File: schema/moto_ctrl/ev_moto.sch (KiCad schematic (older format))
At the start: 131 parts, among them J4 DB37, P7 CONN_6X2, P8 CONN_2, P9 SWD-IAP, Q1 MOSFET_P, Q2 MOSFET_N, Q3 NPN, Q4 MOSFET_P, Q5 NPN, Q6 MOSFET_N, U3 NCP3063, X2 8MHz

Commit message: Made switchable USB.
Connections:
- net labels added: usb-en
- wire segments 457 -> 458
- no-connect marks 17 -> 16

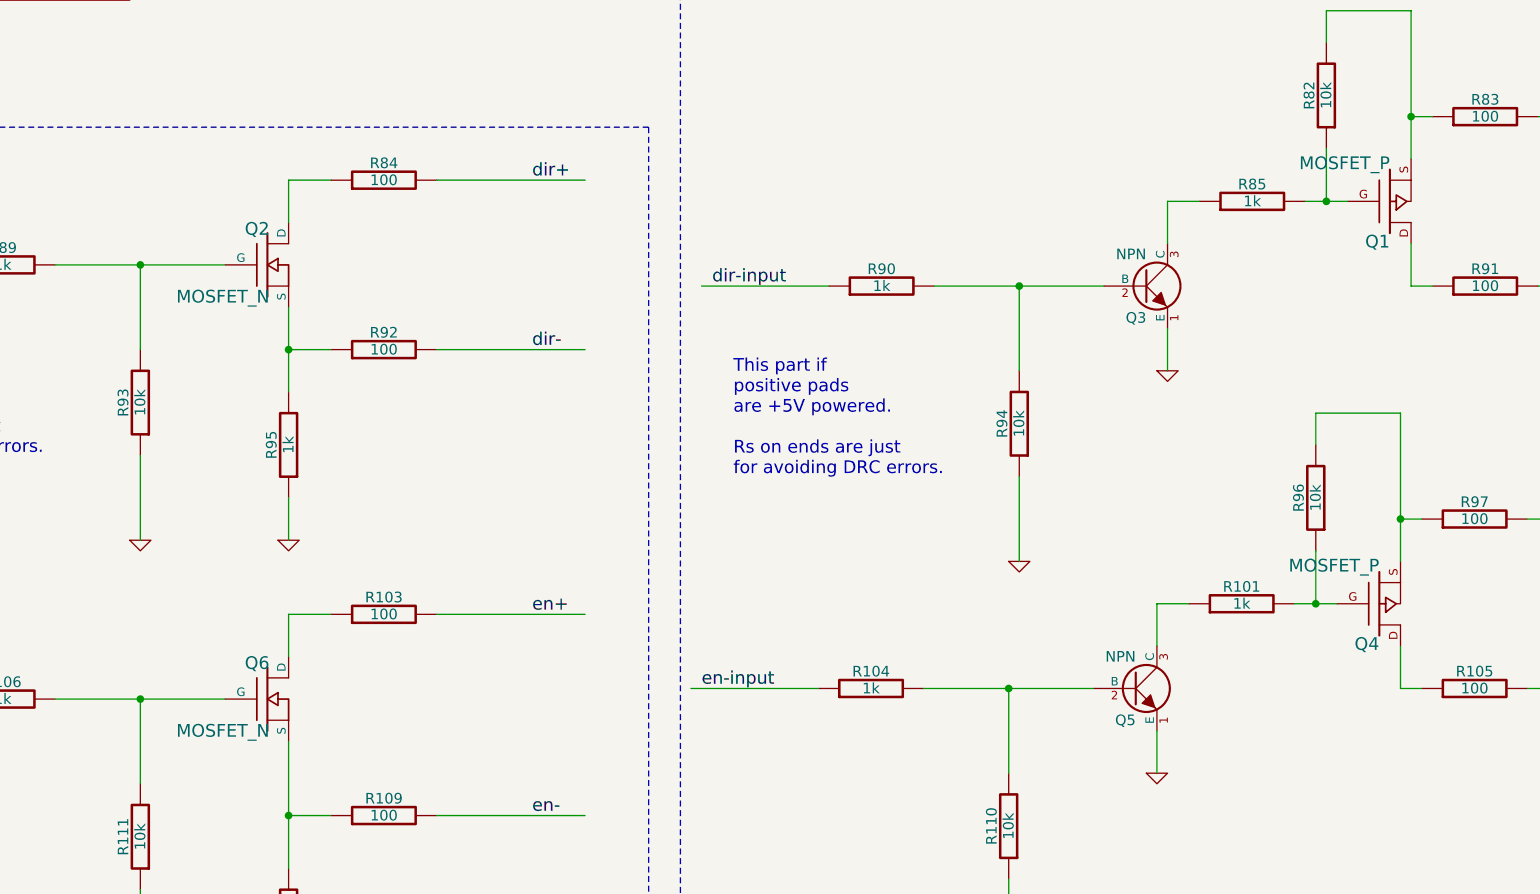
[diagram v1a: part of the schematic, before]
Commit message: Composing bill of materials. And appropriate msfets are chosen for moto_ctrl project.
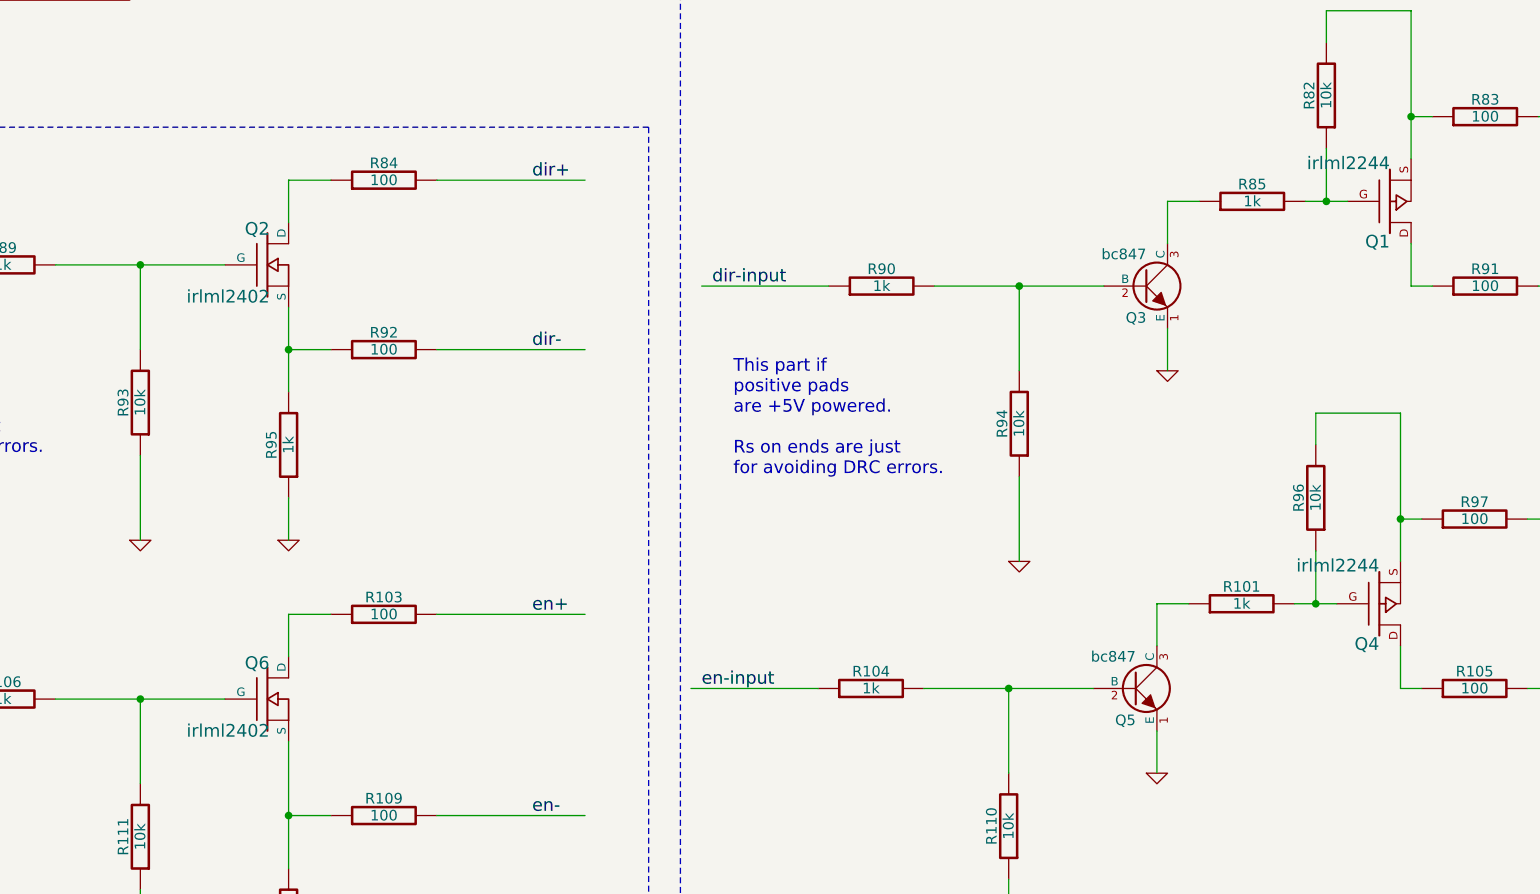
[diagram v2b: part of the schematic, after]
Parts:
- Q1, Q4: value MOSFET_P -> irlml2244
- Q2, Q6: value MOSFET_N -> irlml2402
- Q3, Q5: value NPN -> bc847
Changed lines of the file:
@@
-EESchema Schematic File Version 2  date 22/11/2012 11:04:50
+EESchema Schematic File Version 2  date Wed 05 Dec 2012 08:15:15 PM MSK
 LIBS:power
 LIBS:device
@@
 Sheet 2 2
 Title ""
-Date "22 nov 2012"
+Date "5 dec 2012"
 Rev ""
 Comp ""
@@
 P 13850 13850
 F 0 "Q4" H 13850 14040 60  0000 R CNN
-F 1 "MOSFET_P" H 13850 13670 60  0000 R CNN
+F 1 "irlml2244" H 13850 13670 60  0000 R CNN
 	1    13850 13850
 	1    0    0    1
@@
 P 12700 14250
 F 0 "Q5" H 12700 14100 50  0000 R CNN
-F 1 "NPN" H 12700 14400 50  0000 R CNN
+F 1 "bc847" H 12700 14400 50  0000 R CNN
 	1    12700 14250
 	1    0    0    -1
@@
 P 12750 12350
 F 0 "Q3" H 12750 12200 50  0000 R CNN
-F 1 "NPN" H 12750 12500 50  0000 R CNN
+F 1 "bc847" H 12750 12500 50  0000 R CNN
 	1    12750 12350
 	1    0    0    -1
@@
 P 13900 11950
 F 0 "Q1" H 13900 12140 60  0000 R CNN
-F 1 "MOSFET_P" H 13900 11770 60  0000 R CNN
+F 1 "irlml2244" H 13900 11770 60  0000 R CNN
 	1    13900 11950
 	1    0    0    1
@@
 P 8600 14300
 F 0 "Q6" H 8610 14470 60  0000 R CNN
-F 1 "MOSFET_N" H 8610 14150 60  0000 R CNN
+F 1 "irlml2402" H 8610 14150 60  0000 R CNN
 	1    8600 14300
 	1    0    0    -1
@@
 P 8600 12250
 F 0 "Q2" H 8610 12420 60  0000 R CNN
-F 1 "MOSFET_N" H 8610 12100 60  0000 R CNN
+F 1 "irlml2402" H 8610 12100 60  0000 R CNN
 	1    8600 12250
 	1    0    0    -1
